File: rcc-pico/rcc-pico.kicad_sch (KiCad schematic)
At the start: 44 parts, among them J1 PJ-006A, J10 Conn_02x04_Top_Bottom, J2 Screw_Terminal, J3 Conn_03x3_female, J4 Conn_3x4_female, J5 Conn_03x10, J6 Conn_02x04_Top_Bottom, J7 Conn_02x04_Top_Bottom, J8 Conn_3x3_female, J9 Conn_03x9, Q1 BSS138, Q2 BSS138, Q3 BSS138, SW1 SW_Push, U1 AP63300WU-7, U2 AP2115M-3.3TRG1, U3 PicoW

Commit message: new schematic
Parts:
- removed J3: Conn_03x3_female, Connector_PinHeader_2.54mm:PinHeader3x3_P2.54mm_Vertical, symbol Connector:Conn_03x3_female
- removed J8: Conn_3x3_female, Connector_PinHeader_2.54mm:PinHeader3x3_P2.54mm_Vertical, symbol Connector:Conn_3x3_female
- removed J9: Conn_03x9, 3rdparty:PinHeader3x7+3, symbol Connector:Conn_03x9
- added D?: LED, LED_SMD:LED_0603_1608Metric_Pad1.05x0.95mm_HandSolder, symbol Device:LED
- added J3: Conn_02x04_Odd_Even, PicoShieldHeaders:PinHeader_2x04_P2.54_Vertical_I2C_shunt, symbol Connector_Generic:Conn_02x04_Odd_Even
- added J6: Conn_02x03_Odd_Even, PicoShieldHeaders:PinHeader_2x03_P2.54mm_Vertical, symbol Connector_Generic:Conn_02x03_Odd_Even
- added J7: ~, PicoShieldHeaders:PinHeader_3x04_P2.54mm_Vertical_ServoActivate, symbol Pico_Shield_Headers:Conn_03x04
- added J8, J?: ~, PicoShieldHeaders:PinHeader_3x03_P2.54mm_Vertical_Servo, symbol Pico_Shield_Headers:Conn_03x03
- added J9: Conn_02x07_Odd_Even, Connector_PinHeader_2.54mm:PinHeader_2x07_P2.54mm_Vertical, symbol Connector_Generic:Conn_02x07_Odd_Even
- added R?: 3k, Resistor_SMD:R_0603_1608Metric, symbol Device:R_US
- added R?: PT01-D120K2-B103, Potentiometer:TRIM_PT01-D120K2-B103, symbol Pico_Shield_Headers:PT01-D120K2-B103
- added SW2: SW_Push, Button_Switch_THT:SW_TH_Tactile_Omron_B3F-10xx, symbol Switch:SW_Push
- C3, C7, C8, C9: footprint Capacitor_SMD:C_0402_1005Metric -> Capacitor_SMD:C_0603_1608Metric
- J?: renamed from J10; value Conn_02x04_Top_Bottom -> Conn_02x04_Odd_Even; footprint Connector_PinHeader_2.54mm:PinHeader_2x04_P2.54mm_Vertical-down -> PicoShieldHeaders:PinHeader_2x04_P2.54_Vertical_I2C; symbol Connector_Generic:Conn_02x04_Top_Bottom -> Connector_Generic:Conn_02x04_Odd_Even
- J?: renamed from J7; value Conn_02x04_Top_Bottom -> Conn_02x04_Odd_Even; footprint Connector_PinHeader_2.54mm:PinHeader_2x04_P2.54mm_Vertical-down -> PicoShieldHeaders:PinHeader_2x04_P2.54_Vertical_I2C; symbol Connector_Generic:Conn_02x04_Top_Bottom -> Connector_Generic:Conn_02x04_Odd_Even
- J?: renamed from J6; value Conn_02x04_Top_Bottom -> Conn_02x04_Odd_Even; footprint Connector_PinHeader_2.54mm:PinHeader_2x04_P2.54mm_Vertical -> PicoShieldHeaders:PinHeader_2x04_P2.54_Vertical_I2C_shunt; symbol Connector_Generic:Conn_02x04_Top_Bottom -> Connector_Generic:Conn_02x04_Odd_Even
- R1, R2, R3: footprint Resistor_SMD:R_0402_1005Metric -> Resistor_SMD:R_0603_1608Metric
- R4, R5, R6, R7, R8, R9: footprint Resistor_SMD:R_0402_1005Metric -> Resistor_SMD:R_0603_1608Metric_Pad0.98x0.95mm_HandSolder
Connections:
- net +3.3V: now also J?.7 (Pin_7), J?.7 (Pin_7), Q1.1 (G), Q2.1 (G), Q3.1 (G), J3.5 (Pin_5), J3.6 (Pin_6), J6.3 (Pin_3), J6.4 (Pin_4), J7.4 (Pin_4), J7.5, J7.6, J8.4 (Pin_4), J8.5, J8.6, R?.3; no longer J?.4 (Pin_4), J?.4 (Pin_4)
- net +5V: now also J?.4 (Pin_4), J?.5, J?.6; no longer Q1.1 (G), Q2.1 (G), Q3.1 (G)
- net 3V3_PWM_1: now also J7.10
- net 3V3_PWM_2: now also J7.11
- net 3V3_PWM_3: now also J7.12
- net 5V_PWM_1: now also J?.7
- net 5V_PWM_2: now also J?.8
- net 5V_PWM_3: now also J?.9
- net GND: now also J?.5 (Pin_5), J?.5 (Pin_5), J?.6 (Pin_6), J?.6 (Pin_6), J3.7 (Pin_7), J3.8 (Pin_8), J6.1 (Pin_1), J6.2 (Pin_2), J7.1 (Pin_1), J7.2 (Pin_2), J7.3 (Pin_3), J8.1 (Pin_1), J8.2 (Pin_2), J8.3 (Pin_3), J?.1 (Pin_1), J?.2 (Pin_2), J?.3 (Pin_3), R?.1, R?.2, SW2.2; no longer J?.3 (Pin_3), J?.3 (Pin_3), J?.7 (Pin_7), J?.7 (Pin_7)
- net GPIO16: now also J7.9
- net GPIO17: now also J7.8
- net GPIO18: now also J7.7
- net GPIO19: now also J8.9
- net GPIO20: now also J8.8
- net GPIO21: now also J8.7
- net GPIO22: now also J3.4 (Pin_4)
- net GPIO26: now also J3.3 (Pin_3)
- net GPIO27: now also J6.5 (Pin_5)
- net GPIO28: now also J6.6 (Pin_6)
- net MTRPWR: now also D?.2 (A)
- net SCL: now also J?.3 (Pin_3), J?.3 (Pin_3), J?.4 (Pin_4), J?.4 (Pin_4); no longer J?.2 (Pin_2), J?.2 (Pin_2), J?.6 (Pin_6), J?.6 (Pin_6)
- net SDA: now also J?.2 (Pin_2), J?.2 (Pin_2); no longer J?.5 (Pin_5), J?.5 (Pin_5)
- new net: D?.1 (K), R?.1
- new net POT_signal: J3.1 (Pin_1), R?.2
- new net extra_button: J3.2 (Pin_2), SW2.1
- no-connect marks 7 -> 21
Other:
- note added: "5V PWM activate"
- note added: "ADC1&2"
- note added: "Extra button"
- note added: "GPIO 19-21"
- note added: "I2C1 Activate GPIO 14&15"
- note added: "Motor Indicator LED"
- note added: "Motor POWER"
- note added: "Motor Power"
- note added: "Potentiometer & Button Activate GPIO 22 & 26(ADC0)"
- note added: "Servo Connection (3x3)"
- note added: "Shunt Garage"
- note added: "add fadusials for pick and place"
- note added: "notes: flip switch labels"
- note removed: "I2C1 Activate"
- note removed: "L298N POWER"
- note removed: "L298N Power"
- note removed: "Servo Activate 5V PWM activate"
- note removed: "Servo Connection *note 5V PWM"
- moved on the sheet: C1, C2, C3, C4, C5, C6, C7, C8, C9, D1, H1, H2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

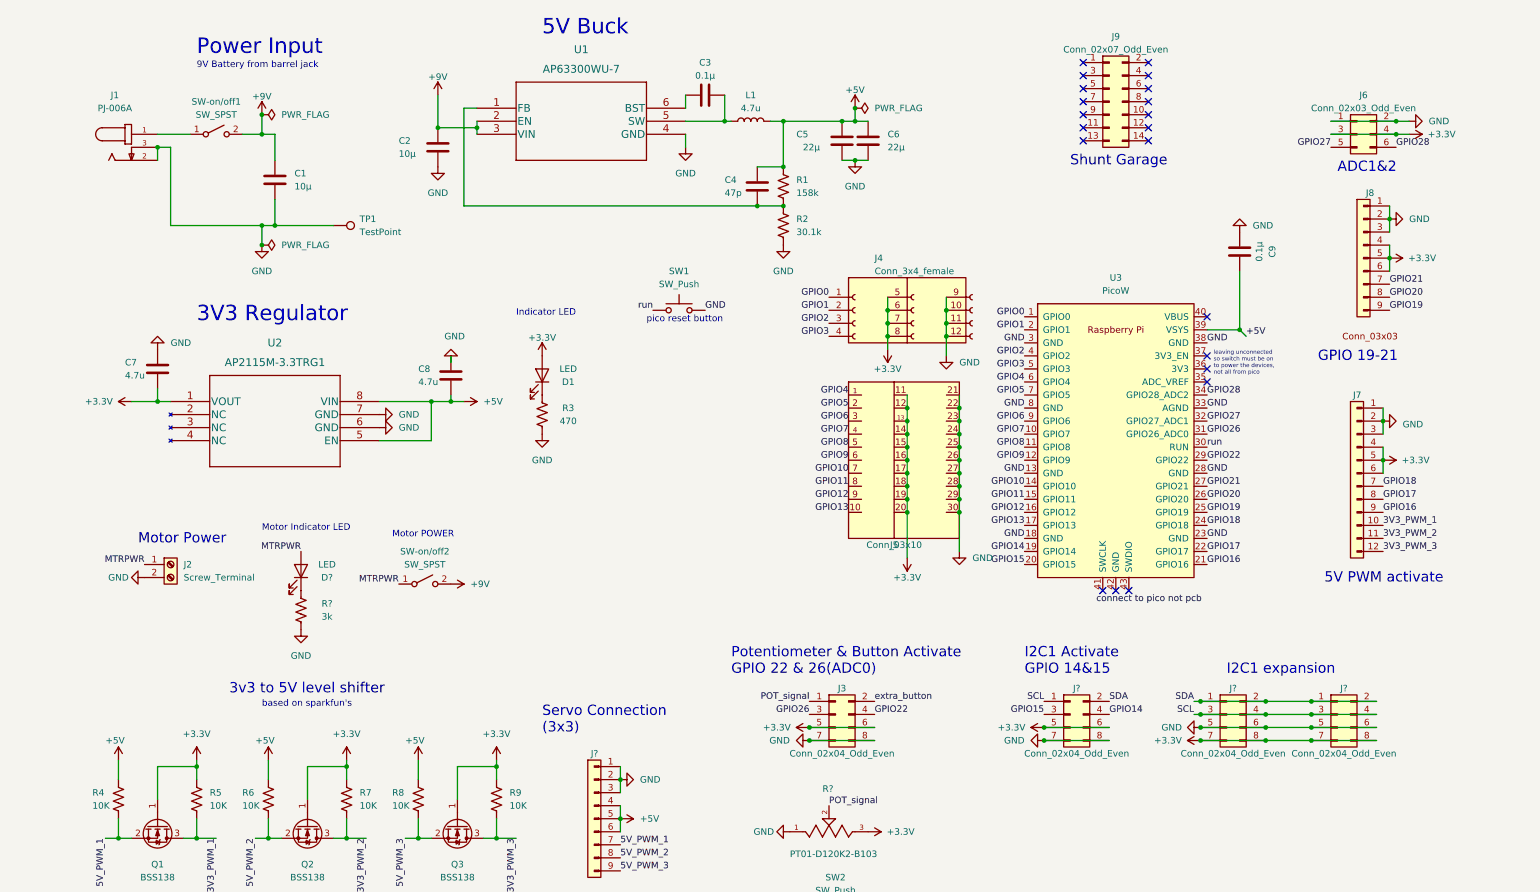
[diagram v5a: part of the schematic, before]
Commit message: new layout and screenprint
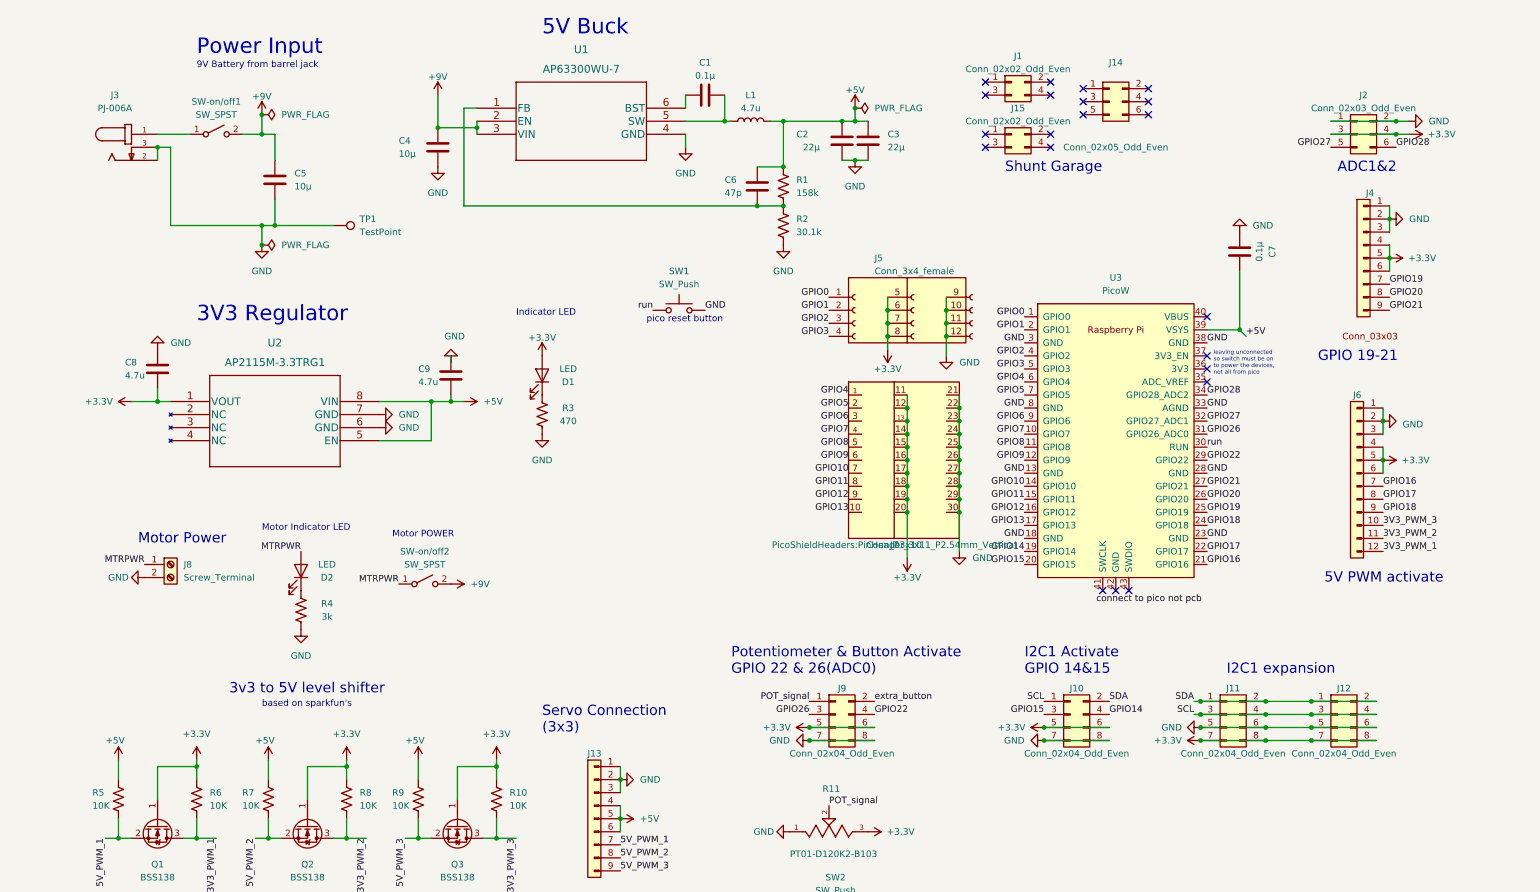
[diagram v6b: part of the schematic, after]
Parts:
- added J1: Conn_02x02_Odd_Even, Connector_PinSocket_2.54mm:PinSocket_1x04_P2.54mm_Vertical, symbol Connector_Generic:Conn_02x02_Odd_Even
- added J15: Conn_02x02_Odd_Even, Connector_PinSocket_2.54mm:PinSocket_2x02_P2.54mm_Vertical, symbol Connector_Generic:Conn_02x02_Odd_Even
- J14: renamed from J9; value Conn_02x07_Odd_Even -> Conn_02x05_Odd_Even; footprint Connector_PinHeader_2.54mm:PinHeader_2x07_P2.54mm_Vertical -> Connector_PinHeader_2.54mm:PinHeader_2x03_P2.54mm_Vertical; symbol Connector_Generic:Conn_02x07_Odd_Even -> Connector_Generic:Conn_02x03_Odd_Even
- J3: renamed from J1; footprint 3rdparty:CUI_PJ-006A -> PicoShieldHeaders:CUI_PJ-006A
- J5: renamed from J4; footprint 3rdparty:PinHeader_3x4_P2.54mm_vertical -> PicoShieldHeaders:PinHeader_3x04_P2.54mm_Vertical_gpio
- J7: renamed from J5; footprint 3rdparty:PinHeader_3x11_P2.54mm_Vertical -> PicoShieldHeaders:PinHeader_3x11_P2.54mm_Vertical
- J8: renamed from J2; footprint TerminalBlock:TCxx03_5mm_2x1 -> PicoShieldHeaders:TCxx03_5mm_2x1
- L1: footprint Inductor_SMD:BWVS00606045 -> PicoShieldHeaders:BWVS00606045
- SW-on/off1, SW-on/off2: footprint 3rdparty:SW-T3-2B-A-A3-S1 -> PicoShieldHeaders:SW-T3-2B-A-A3-S1
- U2: footprint Package_SO:AP2115M-3.3TRG1 -> PicoShieldHeaders:AP2115M-3.3TRG1
- U3: footprint 3rdparty:RPi_Pico_SMD_TH -> PicoShieldHeaders:RPi_Pico_SMD_TH
- gave numbers to parts that had none: 7
- renumbered C3 to C1, C5 to C2, C6 to C3, C2 to C4, C1 to C5, C4 to C6, C9 to C7, C7 to C8, C8 to C9, J6 to J2, J8 to J4, J7 to J6, J3 to J9, R9 to R10, R4 to R5, R5 to R6, R6 to R7, R7 to R8, R8 to R9
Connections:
- net 3V3_PWM_1: now also J6.12; no longer J6.10
- net 3V3_PWM_3: now also J6.10; no longer J6.12
- net GPIO16: now also J6.7; no longer J6.9
- net GPIO18: now also J6.9; no longer J6.7
- net GPIO19: now also J4.7; no longer J4.9
- net GPIO21: now also J4.9; no longer J4.7

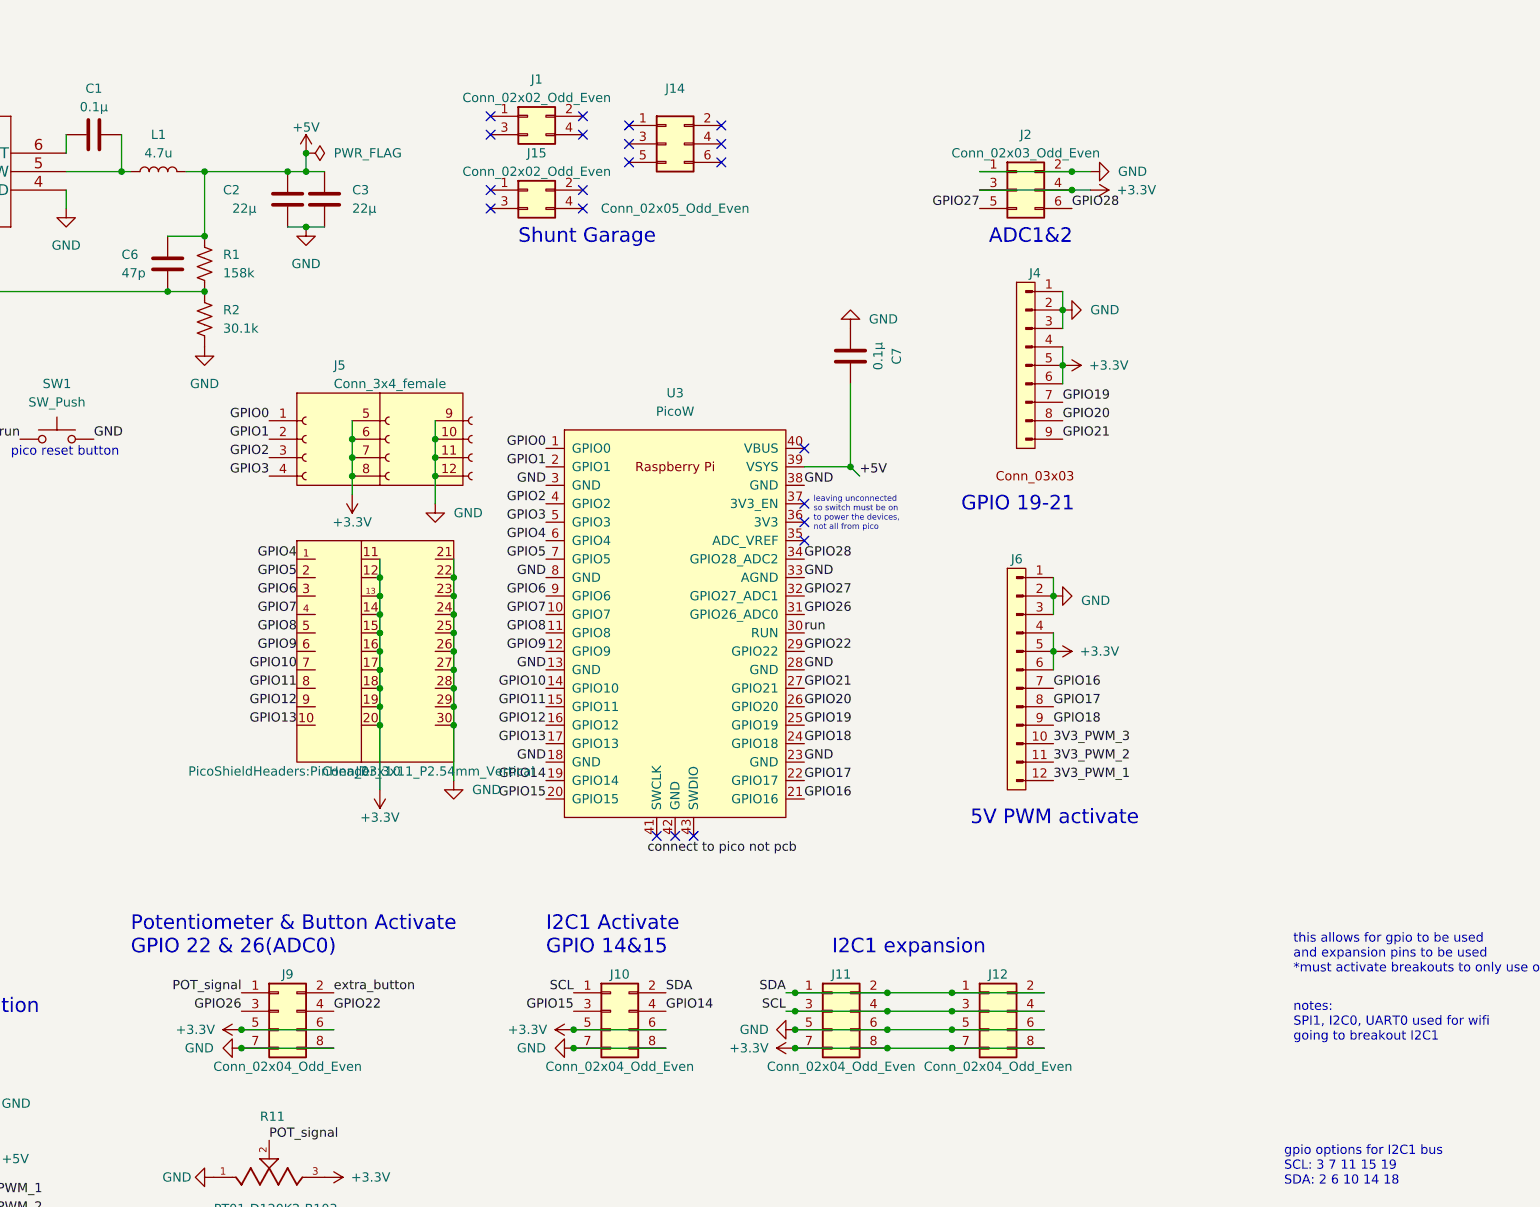
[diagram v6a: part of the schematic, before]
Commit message: finished traces for v0.2
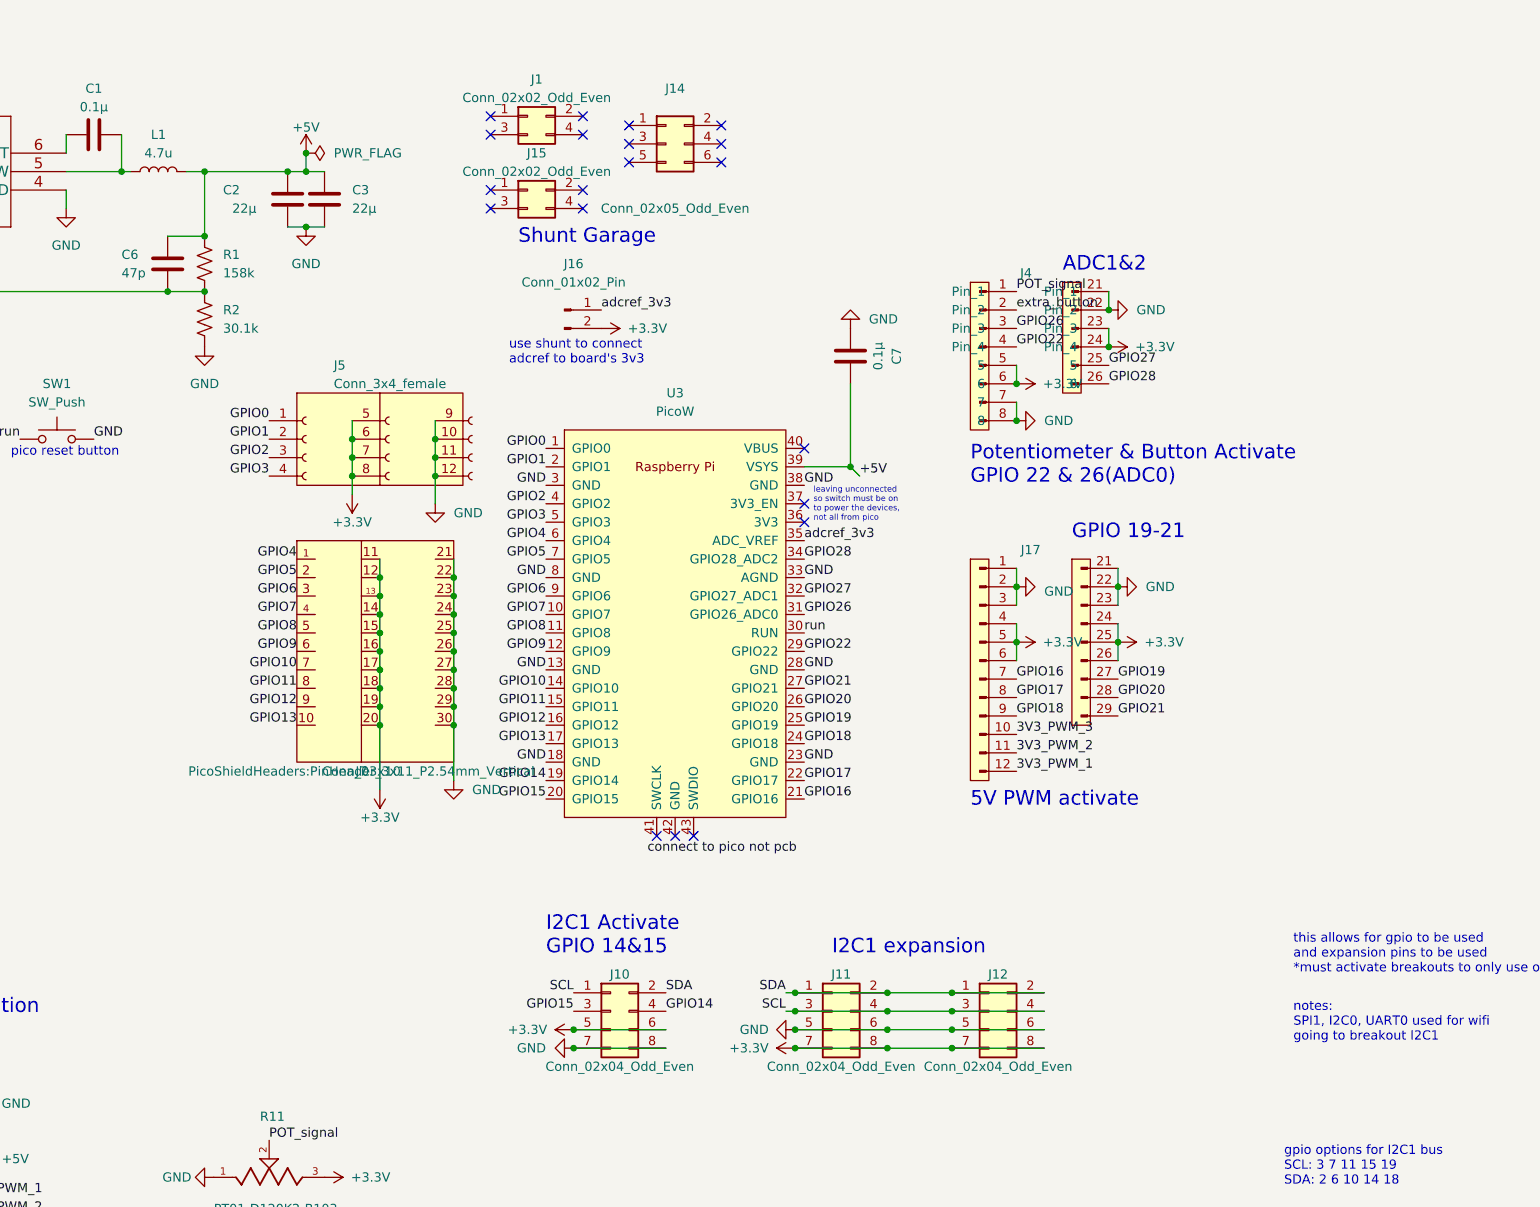
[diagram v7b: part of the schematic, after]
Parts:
- removed J2: Conn_02x03_Odd_Even, PicoShieldHeaders:PinHeader_2x03_P2.54mm_Vertical, symbol Connector_Generic:Conn_02x03_Odd_Even
- removed J4: ~, PicoShieldHeaders:PinHeader_3x03_P2.54mm_Vertical_Servo, symbol Pico_Shield_Headers:Conn_03x03
- removed J6: ~, PicoShieldHeaders:PinHeader_3x04_P2.54mm_Vertical_ServoActivate, symbol Pico_Shield_Headers:Conn_03x04
- removed J9: Conn_02x04_Odd_Even, PicoShieldHeaders:PinHeader_2x04_P2.54_Vertical_I2C_shunt, symbol Connector_Generic:Conn_02x04_Odd_Even
- added J16: Conn_01x02_Pin, Connector_PinHeader_2.54mm:PinHeader_1x02_P2.54mm_Vertical, symbol Connector:Conn_01x02_Pin
- added J17: ~, PicoShieldHeaders:Conn_16-21, symbol Pico_Shield_Headers:Conn_16-21
- added J4: ~, PicoShieldHeaders:Conn_22,24-26, symbol Pico_Shield_Headers:Conn_22,24-26
- SW-on/off1, SW-on/off2: footprint PicoShieldHeaders:SW-T3-2B-A-A3-S1 -> PicoShieldHeaders:SW_OS102011MS2QN1
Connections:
- net +3.3V: now also J16.2 (Pin_2), J17.24 (Pin_4), J17.25 (5), J17.26 (6), J17.4 (Pin_4), J17.5, J17.6, J4.23 (Pin_3), J4.24 (Pin_4), J4.5, J4.6
- net 3V3_PWM_1: now also J17.12
- net 3V3_PWM_2: now also J17.11
- net 3V3_PWM_3: now also J17.10
- net GND: now also J17.1 (Pin_1), J17.2 (Pin_2), J17.21 (Pin_1), J17.22 (Pin_2), J17.23 (Pin_3), J17.3 (Pin_3), J4.21 (Pin_1), J4.22 (Pin_2), J4.7, J4.8
- net GPIO16: now also J17.7
- net GPIO17: now also J17.8
- net GPIO18: now also J17.9
- net GPIO19: now also J17.27 (7)
- net GPIO20: now also J17.28 (8)
- net GPIO21: now also J17.29 (9)
- net GPIO22: now also J4.4 (Pin_4)
- net GPIO26: now also J4.3 (Pin_3)
- net GPIO27: now also J4.25 (5)
- net GPIO28: now also J4.26 (6)
- net POT_signal: now also J4.1 (Pin_1)
- net extra_button: now also J4.2 (Pin_2)
- net adcref_3v3: now reaches U3.35 (ADC_VREF)
- net adcref_3v3: now also J16.1 (Pin_1)
- no-connect marks 21 -> 20
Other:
- note added: "use shunt to connect adcref to board's 3v3"
